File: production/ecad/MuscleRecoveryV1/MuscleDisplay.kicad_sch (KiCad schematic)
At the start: 0 parts

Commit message: Display push attempt
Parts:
- added J5: Conn_01x11_Pin, symbol Connector:Conn_01x11_Pin
- added U6: ESP32-WROOM-32, RF_Module:ESP32-WROOM-32, symbol RF_Module:ESP32-WROOM-32
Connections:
- net MISO: now also J5.5 (Pin_5), U6.31 (IO19)
- net MOSI: now also J5.6 (Pin_6), U6.37 (IO23)
- net SD_CS: now also J5.10 (Pin_10), U6.13 (IO14)
- net TFT_CS: now also J5.7 (Pin_7), U6.23 (IO15)
- net TFT_DC: now also J5.9 (Pin_9), U6.24 (IO2)
- net TFT_RST: now also J5.8 (Pin_8), U6.26 (IO4)
- new net: U6.1 (GND), U6.15 (GND), U6.38 (GND), U6.39 (GND)
- new net +3.3V: J5.2 (Pin_2)
- new net GND: J5.3 (Pin_3)
- new net IO0: U6.25 (IO0)
- new net LIT: J5.11 (Pin_11)
- new net RXD0: U6.34 (RXD0/IO3)
- new net SCK: J5.4 (Pin_4), U6.30 (IO18)
- new net SCL: U6.33 (IO21)
- new net SDA: U6.36 (IO22)
- new net TXD0: U6.35 (TXD0/IO1)
- no-connect marks 0 -> 1

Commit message: Display and Push Button
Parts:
- removed J5: Conn_01x11_Pin, symbol Connector:Conn_01x11_Pin
- removed U6: ESP32-WROOM-32, RF_Module:ESP32-WROOM-32, symbol RF_Module:ESP32-WROOM-32
- added J6: Conn_01x11_Pin, symbol Connector:Conn_01x11_Pin
- added J7: Conn_01x02_Pin, symbol Connector:Conn_01x02_Pin
- added R41: 0, symbol Device:R
- added U8: ESP32-WROOM-32, RF_Module:ESP32-WROOM-32, symbol RF_Module:ESP32-WROOM-32
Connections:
- net +3.3V: now also J6.2 (Pin_2), J7.1 (Pin_1)
- net GND: now also J6.3 (Pin_3)
- net LIT: now also J6.11 (Pin_11), U8.16 (IO13)
- net MISO: now also J6.5 (Pin_5), U8.31 (IO19)
- net MOSI: now also J6.6 (Pin_6), U8.37 (IO23)
- net SCK: now also J6.4 (Pin_4), U8.30 (IO18)
- net SD_CS: now also J6.10 (Pin_10), U8.13 (IO14)
- net TFT_CS: now also J6.7 (Pin_7), U8.23 (IO15)
- net TFT_DC: now also J6.9 (Pin_9), U8.24 (IO2)
- net TFT_RST: now also J6.8 (Pin_8), R41.1
- new net: R41.2, U8.26 (IO4)
- new net: U8.1 (GND), U8.15 (GND), U8.38 (GND), U8.39 (GND)
- new net START_BUTTON: J7.2 (Pin_2), U8.7 (IO35)
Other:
- note added: "Reference MCU"
- note added: "START BUTTON GPIO"
- note added: "TFT SCREEN CONNECTOR *include SPI bus for SD Card and TFT screen - SCK - miso (only for SD card) - mosi - SD_CS & TFT_CS"

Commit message: rev1 first draft ready for review
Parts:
- removed R41: 0, symbol Device:R
- removed U8: ESP32-WROOM-32, RF_Module:ESP32-WROOM-32, symbol RF_Module:ESP32-WROOM-32
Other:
- note removed: "Reference MCU"

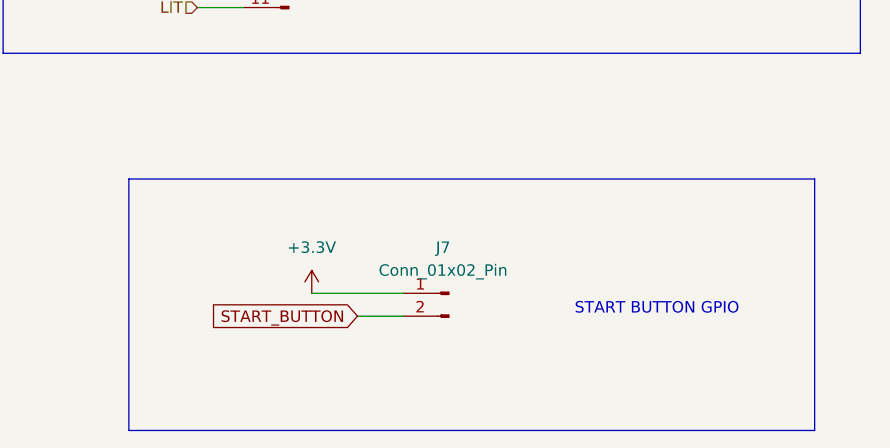
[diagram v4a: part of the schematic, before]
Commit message: Footprints added
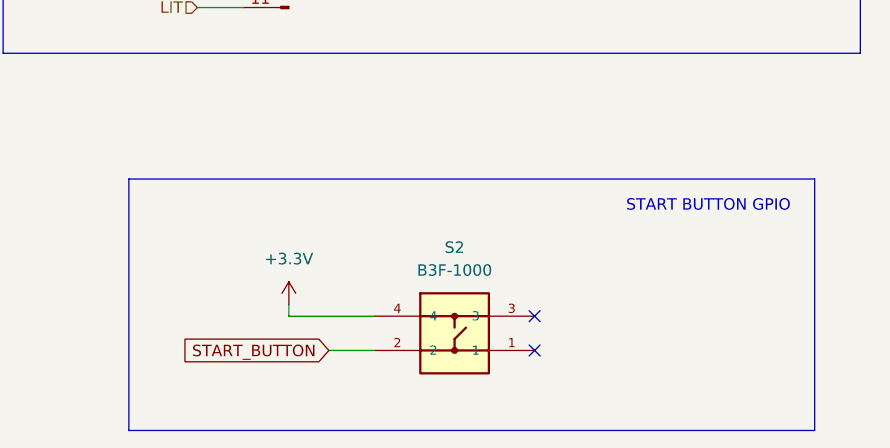
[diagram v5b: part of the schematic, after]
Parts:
- removed J7: Conn_01x02_Pin, symbol Connector:Conn_01x02_Pin
- added S2: B3F-1000, B3F-1000:SW_B3F-1000, symbol B3F-1000:B3F-1000
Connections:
- net +3.3V: now also S2.4
- net START_BUTTON: now also S2.2
- no-connect marks 1 -> 3
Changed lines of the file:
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@@
     (company "Generate Product Development Studio")
   )
+  (no_connect (at 216.535 133.35))
   (no_connect (at 184.15 73.66))
+  (no_connect (at 216.535 137.16))
   (wire (pts (xy 179.07 99.06) (xy 184.15 99.06))
     (stroke (width 0) (type default))
@@
     (stroke (width 0) (type default))
   )
-  (wire (pts (xy 196.85 133.35) (xy 201.93 133.35))
-    (stroke (width 0) (type default))
-  )
-  (wire (pts (xy 191.77 130.81) (xy 201.93 130.81))
+  (wire (pts (xy 193.675 137.16) (xy 198.755 137.16))
+    (stroke (width 0) (type default))
+  )
+  (wire (pts (xy 189.23 133.35) (xy 198.755 133.35))
     (stroke (width 0) (type default))
   )
@@
   )
   (wire (pts (xy 179.07 88.9) (xy 184.15 88.9))
+    (stroke (width 0) (type default))
+  )
+  (wire (pts (xy 189.23 132.08) (xy 189.23 133.35))
     (stroke (width 0) (type default))
   )
@@
     (effects (font (size 1.27 1.27)) (justify left bottom))
   )
-  (text "START BUTTON GPIO\n" (at 220.98 133.35 0)
+  (text "START BUTTON GPIO\n" (at 226.695 121.92 0)
     (effects (font (size 1.27 1.27)) (justify left bottom))
   )
-  (global_label "START_BUTTON" (shape input) (at 196.85 133.35 180) (fields_autoplaced)
-    (effects (font (size 1.27 1.27)) (justify right))
-    (property "Intersheetrefs" "${INTERSHEET_REFS}" (at 180.1972 133.35 0)
+  (global_label "START_BUTTON" (shape input) (at 193.675 137.16 180) (fields_autoplaced)
+    (effects (font (size 1.27 1.27)) (justify right))
+    (property "Intersheetrefs" "${INTERSHEET_REFS}" (at 177.0222 137.16 0)
       (effects (font (size 1.27 1.27)) (justify right) hide)
     )
@@
     )
   )
-  (symbol (lib_id "Connector:Conn_01x02_Pin") (at 207.01 130.81 0) (mirror y) (unit 1)
-    (in_bom yes) (on_board yes) (dnp no)
-    (property "Reference" "J7" (at 206.375 125.73 0)
-      (effects (font (size 1.27 1.27)))
-    )
-    (property "Value" "Conn_01x02_Pin" (at 206.375 128.27 0)
-      (effects (font (size 1.27 1.27)))
-    )
-    (property "Footprint" "" (at 207.01 130.81 0)
-      (effects (font (size 1.27 1.27)) hide)
-    )
-    (property "Datasheet" "~" (at 207.01 130.81 0)
-      (effects (font (size 1.27 1.27)) hide)
+  (symbol (lib_id "power:+3.3V") (at 166.37 76.2 0) (unit 1)
+    (in_bom yes) (on_board yes) (dnp no) (fields_autoplaced)
+    (property "Reference" "#PWR060" (at 166.37 80.01 0)
+      (effects (font (size 1.27 1.27)) hide)
+    )
+    (property "Value" "+3.3V" (at 166.37 71.12 0)
+      (effects (font (size 1.27 1.27)))
+    )
+    (property "Footprint" "" (at 166.37 76.2 0)
+      (effects (font (size 1.27 1.27)) hide)
+    )
+    (property "Datasheet" "" (at 166.37 76.2 0)
+      (effects (font (size 1.27 1.27)) hide)
+    )
+    (pin "1")
+    (instances
+      (project "MuscleRecoveryV1"
+        (path "/4e550305-79d2-4e4a-a502-817ebcc79f9a/85edd68f-6119-4dbf-9af0-99f996378c09"
+          (reference "#PWR060") (unit 1)
+        )
+      )
+    )
+  )
+  (symbol (lib_id "power:+3.3V") (at 189.23 132.08 0) (unit 1)
+    (in_bom yes) (on_board yes) (dnp no) (fields_autoplaced)
+    (property "Reference" "#PWR062" (at 189.23 135.89 0)
+      (effects (font (size 1.27 1.27)) hide)
+    )
+    (property "Value" "+3.3V" (at 189.23 127 0)
+      (effects (font (size 1.27 1.27)))
+    )
+    (property "Footprint" "" (at 189.23 132.08 0)
+      (effects (font (size 1.27 1.27)) hide)
+    )
+    (property "Datasheet" "" (at 189.23 132.08 0)
+      (effects (font (size 1.27 1.27)) hide)
+    )
+    (pin "1")
+    (instances
+      (project "MuscleRecoveryV1"
+        (path "/4e550305-79d2-4e4a-a502-817ebcc79f9a/85edd68f-6119-4dbf-9af0-99f996378c09"
+          (reference "#PWR062") (unit 1)
+        )
+      )
+    )
+  )
+  (symbol (lib_id "B3F-1000:B3F-1000") (at 207.645 138.43 0) (unit 1)
+    (in_bom yes) (on_board yes) (dnp no) (fields_autoplaced)
+    (property "Reference" "S2" (at 207.6434 125.73 0)
+      (effects (font (size 1.27 1.27)))
+    )
+    (property "Value" "B3F-1000" (at 207.6434 128.27 0)
+      (effects (font (size 1.27 1.27)))
+    )
+    (property "Footprint" "B3F-1000:SW_B3F-1000" (at 212.725 157.48 0)
+      (effects (font (size 1.27 1.27)) (justify bottom) hide)
+    )
+    (property "Datasheet" "" (at 207.645 143.51 0)
+      (effects (font (size 1.27 1.27)) hide)
+    )
+    (property "MF" "Omron" (at 207.645 143.51 0)
+      (effects (font (size 1.27 1.27)) (justify bottom) hide)
+    )
+    (property "Description" "\nTactile Switch SPST-NO Top Actuated Through Hole\n" (at 203.835 168.91 0)
+      (effects (font (size 1.27 1.27)) (justify bottom) hide)
+    )
+    (property "Package" "None" (at 207.645 143.51 0)
+      (effects (font (size 1.27 1.27)) (justify bottom) hide)
+    )
+    (property "Price" "None" (at 207.645 143.51 0)
+      (effects (font (size 1.27 1.27)) (justify bottom) hide)
+    )
+    (property "Check_prices" "https://www.snapeda.com/parts/B3F-1000/Omron+Electronics+Inc-EMC+Div/view-part/?ref=eda" (at 212.725 157.48 0)
+      (effects (font (size 1.27 1.27)) (justify bottom) hide)
+    )
+    (property "SnapEDA_Link" "https://www.snapeda.com/parts/B3F-1000/Omron+Electronics+Inc-EMC+Div/view-part/?ref=snap" (at 212.725 157.48 0)
+      (effects (font (size 1.27 1.27)) (justify bottom) hide)
+    )
+    (property "MP" "B3F-1000" (at 207.645 143.51 0)
+      (effects (font (size 1.27 1.27)) (justify bottom) hide)
+    )
+    (property "Purchase-URL" "https://www.snapeda.com/api/url_track_click_mouser/?unipart_id=48569&manufacturer=Omron&part_name=B3F-1000&search_term=b3f-10" (at 203.835 168.91 0)
+      (effects (font (size 1.27 1.27)) (justify bottom) hide)
+    )
+    (property "Availability" "In Stock" (at 207.645 143.51 0)
+      (effects (font (size 1.27 1.27)) (justify bottom) hide)
+    )
+    (property "MANUFACTURER" "Omron" (at 207.645 143.51 0)
+      (effects (font (size 1.27 1.27)) (justify bottom) hide)
     )
     (pin "1")
     (pin "2")
-    (instances
-      (project "MuscleRecoveryV1"
-        (path "/4e550305-79d2-4e4a-a502-817ebcc79f9a/85edd68f-6119-4dbf-9af0-99f996378c09"
-          (reference "J7") (unit 1)
-        )
-      )
-    )
-  )
-  (symbol (lib_id "power:+3.3V") (at 166.37 76.2 0) (unit 1)
-    (in_bom yes) (on_board yes) (dnp no) (fields_autoplaced)
-    (property "Reference" "#PWR060" (at 166.37 80.01 0)
-      (effects (font (size 1.27 1.27)) hide)
-    )
-    (property "Value" "+3.3V" (at 166.37 71.12 0)
-      (effects (font (size 1.27 1.27)))
-    )
-    (property "Footprint" "" (at 166.37 76.2 0)
-      (effects (font (size 1.27 1.27)) hide)
-    )
-    (property "Datasheet" "" (at 166.37 76.2 0)
-      (effects (font (size 1.27 1.27)) hide)
-    )
-    (pin "1")
-    (instances
-      (project "MuscleRecoveryV1"
-        (path "/4e550305-79d2-4e4a-a502-817ebcc79f9a/85edd68f-6119-4dbf-9af0-99f996378c09"
-          (reference "#PWR060") (unit 1)
-        )
-      )
-    )
-  )
-  (symbol (lib_id "power:+3.3V") (at 191.77 130.81 0) (unit 1)
-    (in_bom yes) (on_board yes) (dnp no) (fields_autoplaced)
-    (property "Reference" "#PWR062" (at 191.77 134.62 0)
-      (effects (font (size 1.27 1.27)) hide)
-    )
-    (property "Value" "+3.3V" (at 191.77 125.73 0)
-      (effects (font (size 1.27 1.27)))
-    )
-    (property "Footprint" "" (at 191.77 130.81 0)
-      (effects (font (size 1.27 1.27)) hide)
-    )
-    (property "Datasheet" "" (at 191.77 130.81 0)
-      (effects (font (size 1.27 1.27)) hide)
-    )
-    (pin "1")
-    (instances
-      (project "MuscleRecoveryV1"
-        (path "/4e550305-79d2-4e4a-a502-817ebcc79f9a/85edd68f-6119-4dbf-9af0-99f996378c09"
-          (reference "#PWR062") (unit 1)
-        )
-      )
+    (pin "3")
+    (pin "4")
+    (instances
+      (project "MuscleRecoveryV1"
+        (path "/4e550305-79d2-4e4a-a502-817ebcc79f9a/50c43c35-6798-4b23-b9a6-29e92679e65f"
+          (reference "S2") (unit 1)
+        )
+        (path "/4e550305-79d2-4e4a-a502-817ebcc79f9a/85edd68f-6119-4dbf-9af0-99f996378c09"
+          (reference "S1") (unit 1)
+        )
+      )

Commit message: Maggie fixing her mistakes lol
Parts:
- removed J6: Conn_01x11_Pin, symbol Connector:Conn_01x11_Pin
- added J7: Conn_01x11_Pin, symbol Connector:Conn_01x11_Pin
- added R35, R50, R51, R52, R53, R54, R55, R56: 0, symbol Device:R_Small
- added R57, R58: 10k, symbol Device:R_Small
- added S4: B3F-1000, B3F-1000:SW_B3F-1000, symbol B3F-1000:B3F-1000
- renumbered S2 to S1
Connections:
- net +3.3V: now also J7.2 (Pin_2), S4.4
- net GND: now also J7.3 (Pin_3), R57.2, R58.2
- net LIT: now also R56.1
- net MISO: now also R50.1
- net MOSI: now also R51.1
- net SCK: now also R35.1
- net SD_CS: now also R55.1
- net START_BUTTON: now also R57.1
- net TFT_CS: now also R52.1
- net TFT_DC: now also R54.1
- net TFT_RST: now also R53.1
- new net: J7.4 (Pin_4), R35.2
- new net: J7.11 (Pin_11), R56.2
- new net: J7.8 (Pin_8), R53.2
- new net: J7.7 (Pin_7), R52.2
- new net: J7.9 (Pin_9), R54.2
- new net: J7.5 (Pin_5), R50.2
- new net: J7.10 (Pin_10), R55.2
- new net: J7.6 (Pin_6), R51.2
- new net ALT_START_BUTTON: R58.1, S4.2
- no-connect marks 3 -> 5
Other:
- note added: "ALT START BUTTON GPIO"
- note added: "TFT SCREEN CONNECTOR *include SPI bus for SD Card & TFT screen - SCK - miso (only for SD card) - mosi - SD_CS & TFT_CS"
- note removed: "TFT SCREEN CONNECTOR *include SPI bus for SD Card and TFT screen - SCK - miso (only for SD card) - mosi - SD_CS & TFT_CS"
- moved on the sheet: S1

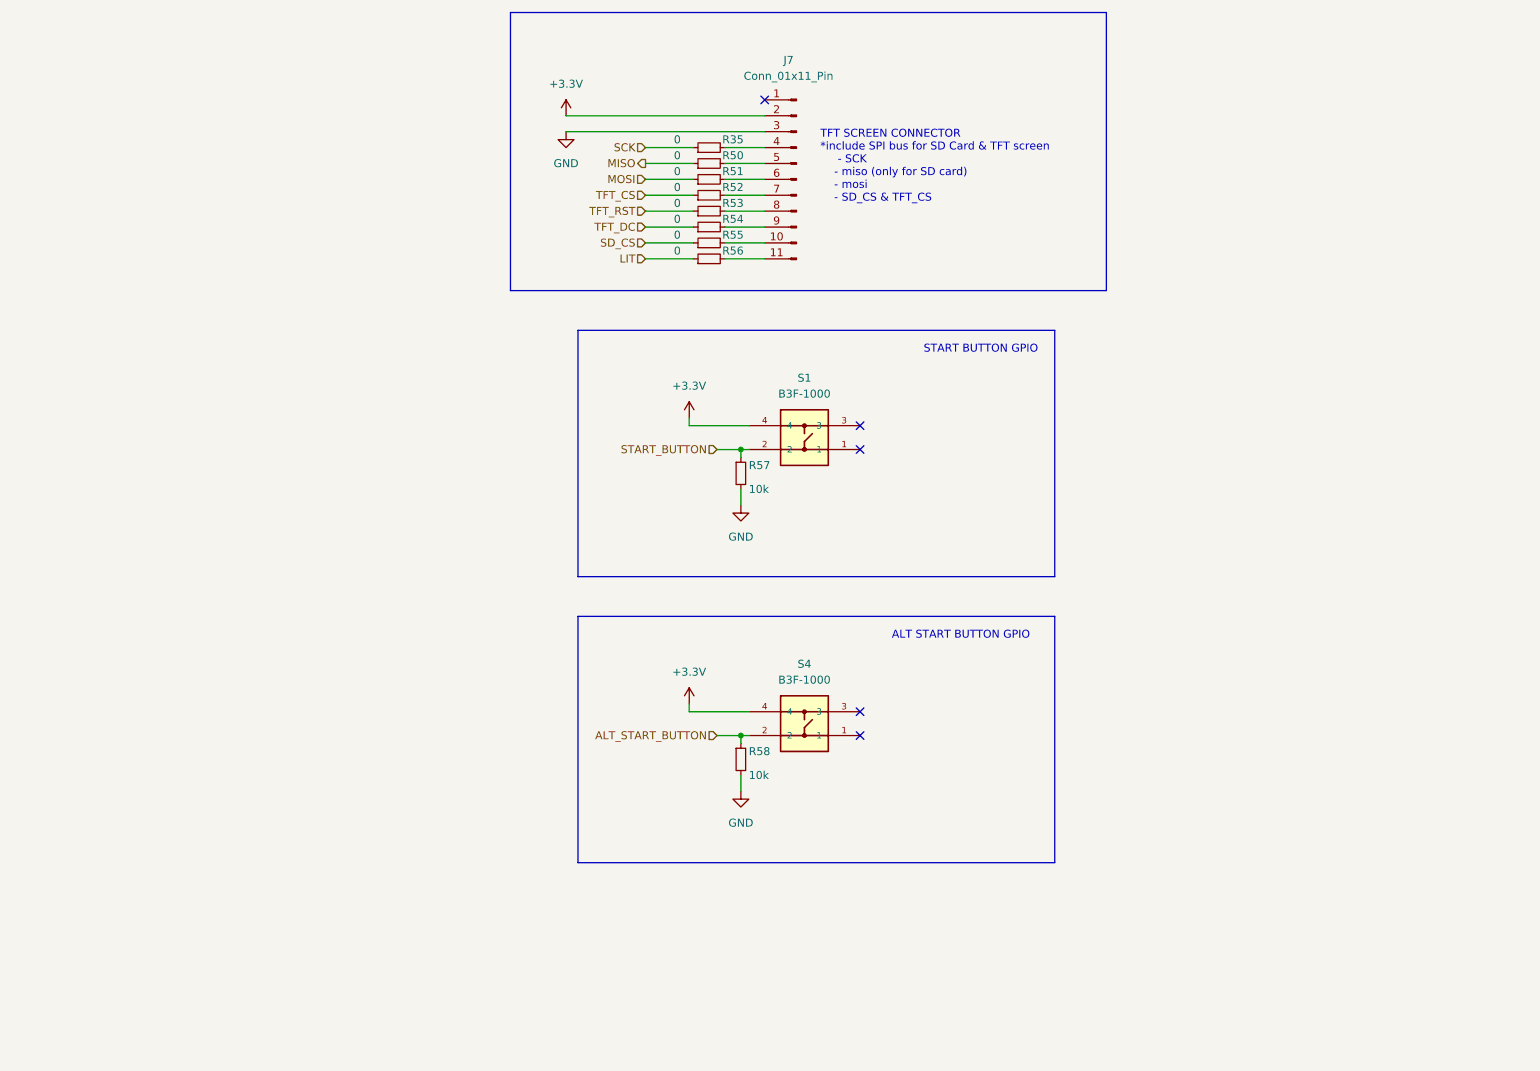
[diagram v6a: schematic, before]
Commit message: Adding Motor Circuitry
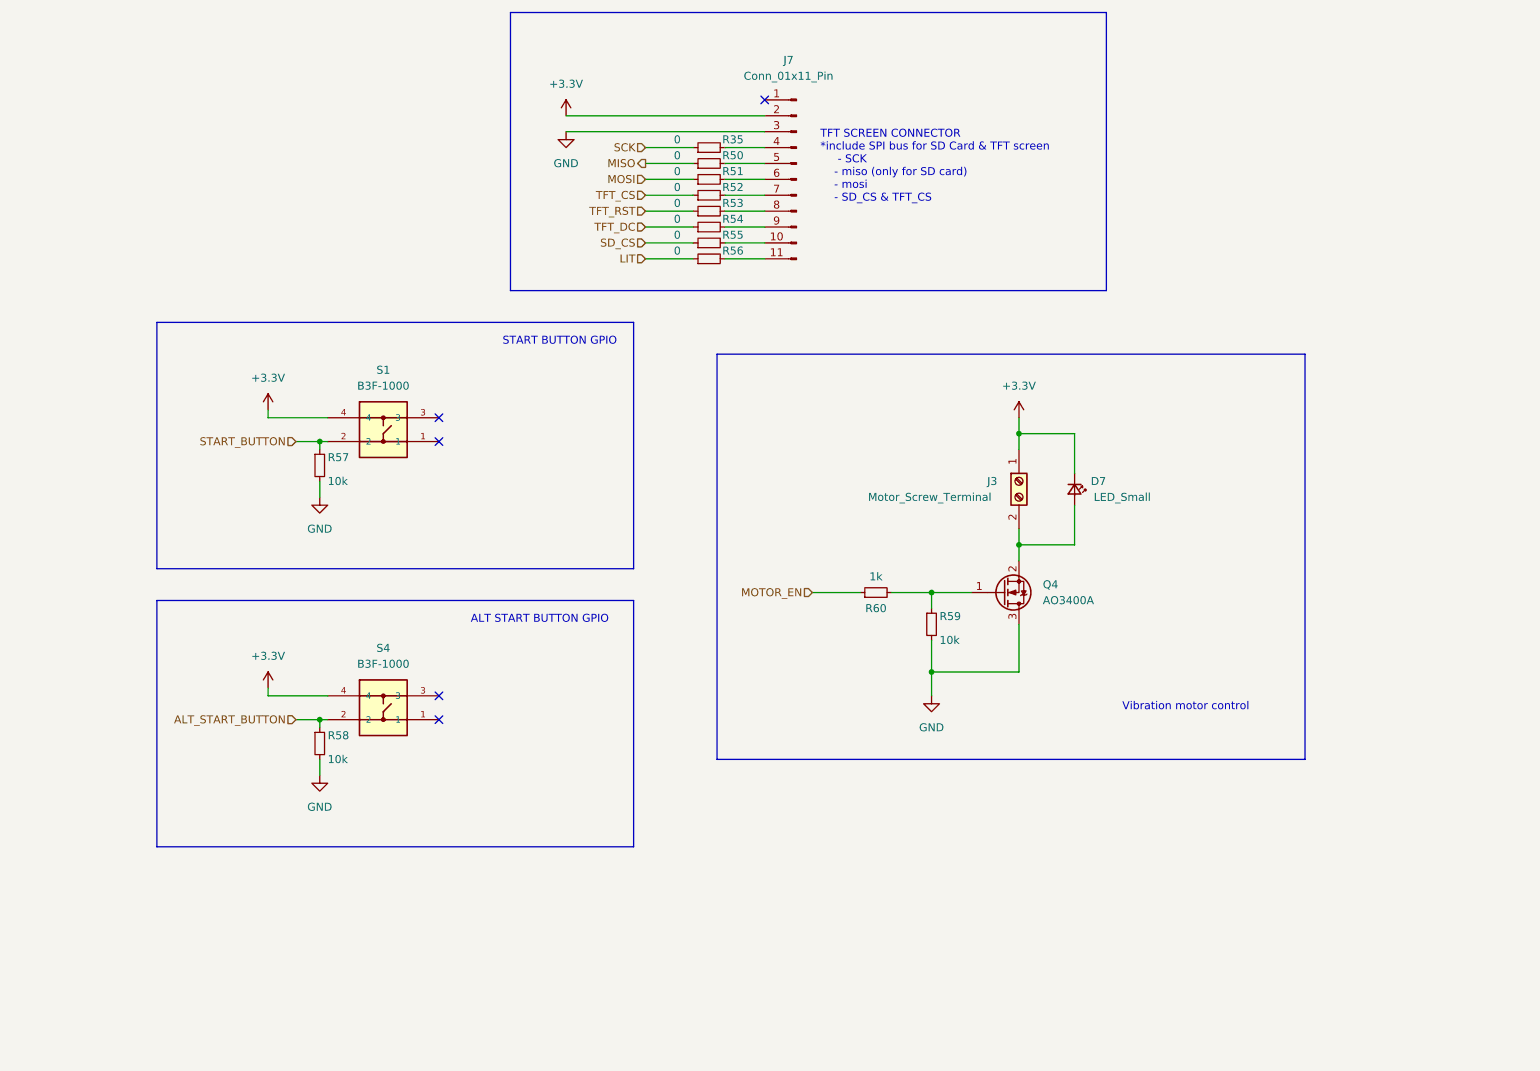
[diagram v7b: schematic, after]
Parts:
- added D7: LED_Small, LED_THT:LED_D1.8mm_W3.3mm_H2.4mm, symbol Device:LED_Small
- added J3: Motor_Screw_Terminal, symbol Connector:Screw_Terminal_01x02
- added Q4: AO3400A, Package_TO_SOT_SMD:SOT-23, symbol Transistor_FET:AO3400A
- added R59: 10k, symbol Device:R_Small
- added R60: 1k, symbol Device:R_Small
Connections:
- net +3.3V: now also D7.1 (K), J3.1 (Pin_1)
- net GND: now also Q4.3 (D), R59.2
- new net: D7.2 (A), J3.2 (Pin_2), Q4.2 (S)
- new net: Q4.1 (G), R59.1, R60.2
- new net MOTOR_EN: R60.1
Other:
- note added: "Vibration motor control"
- moved on the sheet: R57, R58, S1, S4
